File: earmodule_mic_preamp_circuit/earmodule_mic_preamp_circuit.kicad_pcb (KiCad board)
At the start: 2 copper layers, 43.8 x 25.4 mm, 53 parts, among them CN1 22uF, U100 AD8476ARMZ, U200 AD8476ARMZ, U300 ADA4661-2ARMZ, U400 TITLV71210

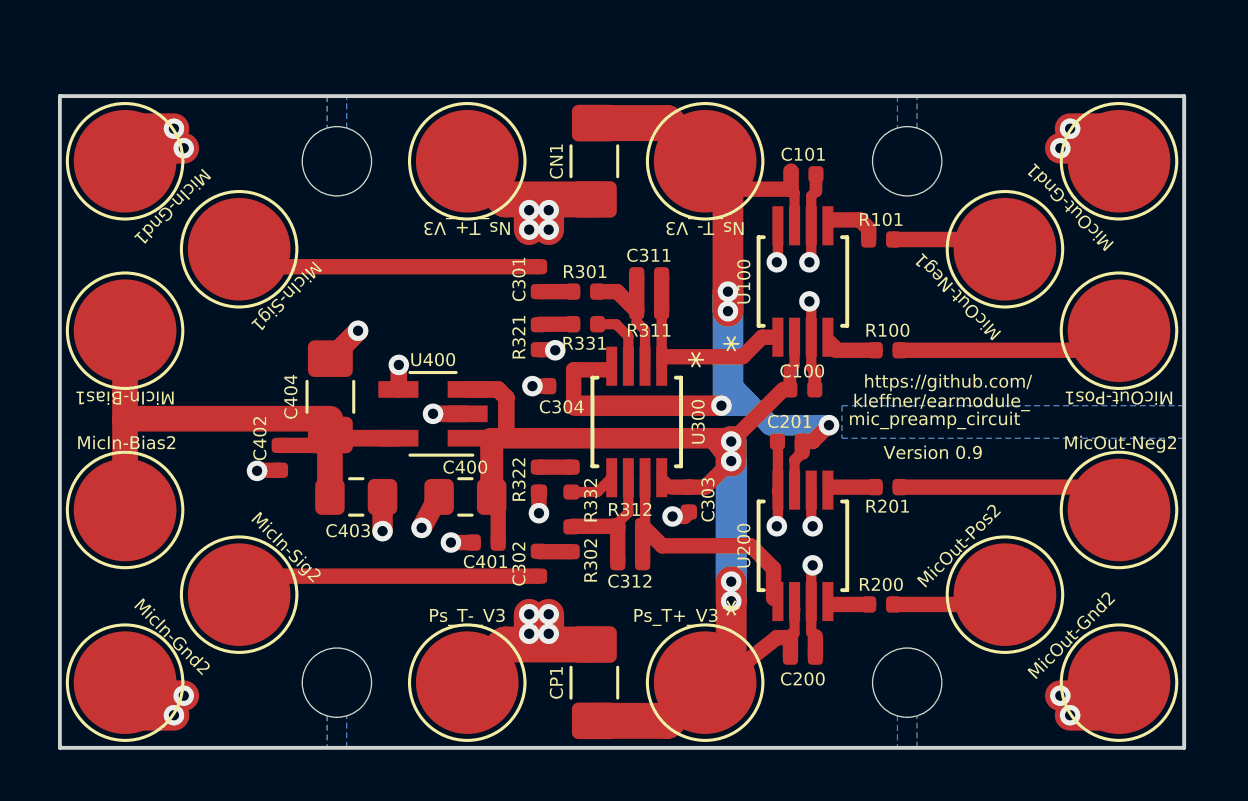
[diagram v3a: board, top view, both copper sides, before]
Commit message: Corrected miminum solder mask width. Aligned traces and copper fill along board edge to statisfy minimums. Removed backup file from repo.
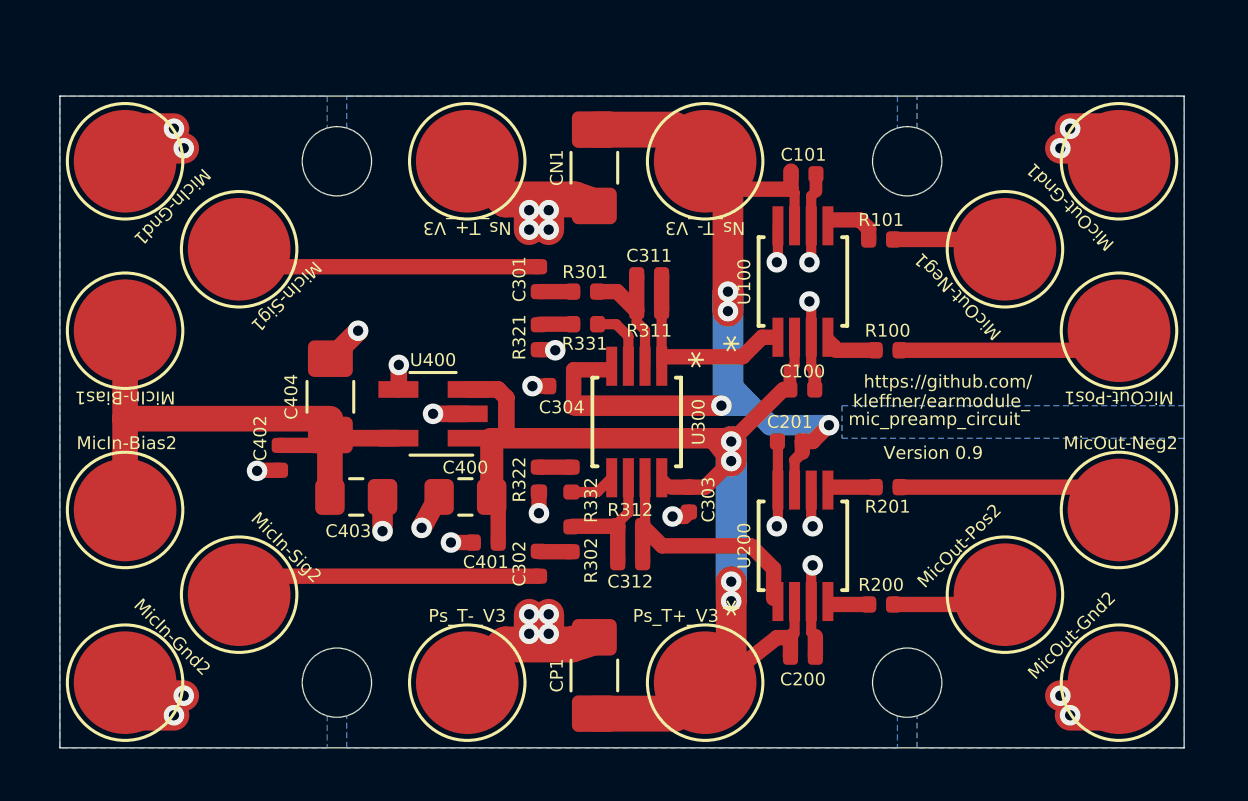
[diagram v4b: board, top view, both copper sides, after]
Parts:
- moved CP1 0.28 mm to (126.5, 94.5)
- moved CN1 0.25 mm to (126.5, 74.7)
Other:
- rule solder_mask_min_width: 0.25 -> 0.1016
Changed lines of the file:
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@@
     (thickness 1.6)
     (drawings 8)
-    (tracks 212)
+    (tracks 210)
     (zones 0)
     (modules 53)
@@
     (trace_min 0.2)
     (segment_width 0.2)
-    (edge_width 0.15)
+    (edge_width 0.05)
     (via_size 0.8)
     (via_drill 0.4)
@@
     (pad_drill 2.7)
     (pad_to_mask_clearance 0.051)
-    (solder_mask_min_width 0.25)
+    (solder_mask_min_width 0.1016)
     (aux_axis_origin 0 0)
     (visible_elements FFFDFF7F)
@@
   )
   (module Capacitor_SMD:C_1206_3216Metric_Pad1.42x1.75mm_HandSolder (layer F.Cu)
-    (at 126.492 74.422 90)
+    (at 126.492 74.676 90)
     (descr "Capacitor SMD 1206 (3216 Metric), square (rectangular) end terminal, IPC_7351 nominal with elongated pad for handsoldering. (Body size source: http://www.tortai-tech.com/upload/download/2011102023233369053.pdf), generated with kicad-footprint-generator")
     (tags "capacitor handsolder")
@@
   )
   (module Capacitor_SMD:C_1206_3216Metric_Pad1.42x1.75mm_HandSolder (layer F.Cu)
-    (at 126.492 94.742 90)
+    (at 126.492 94.461 90)
     (descr "Capacitor SMD 1206 (3216 Metric), square (rectangular) end terminal, IPC_7351 nominal with elongated pad for handsoldering. (Body size source: http://www.tortai-tech.com/upload/download/2011102023233369053.pdf), generated with kicad-footprint-generator")
     (tags "capacitor handsolder")
@@
     (effects (font (size 0.5 0.5) (thickness 0.0625)))
   )
-  (gr_line (start 149.479 71.882) (end 105.664 71.882) (layer Edge.Cuts) (width 0.15))
-  (gr_line (start 149.479 97.282) (end 149.479 71.882) (layer Edge.Cuts) (width 0.15))
-  (gr_line (start 105.664 97.282) (end 149.479 97.282) (layer Edge.Cuts) (width 0.15))
-  (gr_line (start 105.664 71.882) (end 105.664 97.282) (layer Edge.Cuts) (width 0.15))
+  (gr_line (start 149.479 71.882) (end 105.664 71.882) (layer Edge.Cuts) (width 0.05))
+  (gr_line (start 149.479 97.282) (end 149.479 71.882) (layer Edge.Cuts) (width 0.05))
+  (gr_line (start 105.664 97.282) (end 149.479 97.282) (layer Edge.Cuts) (width 0.05))
+  (gr_line (start 105.664 71.882) (end 105.664 97.282) (layer Edge.Cuts) (width 0.05))
   (segment (start 124.333 79.502) (end 125.649 79.502) (width 0.6) (layer F.Cu) (net 1))
   (segment (start 125.603 89.639) (end 124.333 89.639) (width 0.6) (layer F.Cu) (net 2))
@@
   (segment (start 137.183 77.05) (end 136.841 76.708) (width 0.6) (layer F.Cu) (net 8))
   (segment (start 137.183 77.47) (end 137.183 77.05) (width 0.6) (layer F.Cu) (net 8))
-  (segment (start 135.709299 91.694) (end 135.594999 91.5797) (width 0.4) (layer F.Cu) (net 9))
   (segment (start 137.183 91.694) (end 135.709299 91.694) (width 0.6) (layer F.Cu) (net 9))
-  (segment (start 135.709299 87.122) (end 135.594999 87.2363) (width 0.4) (layer F.Cu) (net 10))
   (segment (start 137.437 87.122) (end 135.709299 87.122) (width 0.6) (layer F.Cu) (net 10))
   (segment (start 124.356 80.772) (end 124.333 80.795) (width 0.4) (layer F.Cu) (net 11))
@@
   (segment (start 130.175 87.122) (end 130.81 87.122) (width 0.6) (layer F.Cu) (net 15))
   (segment (start 134.294999 92.827001) (end 134.294999 91.919665) (width 0.4) (layer F.Cu) (net 15))
-  (segment (start 134.294999 91.919665) (end 134.3291 91.885564) (width 0.4) (layer F.Cu) (net 15))
-  (segment (start 129.3225 96.2295) (end 130.81 94.742) (width 1.4) (layer F.Cu) (net 15))
-  (segment (start 126.492 96.2295) (end 129.3225 96.2295) (width 1.4) (layer F.Cu) (net 15))
   (segment (start 134.079001 92.964) (end 134.239 92.827001) (width 0.5) (layer F.Cu) (net 15))
   (segment (start 134.079001 92.987) (end 134.079001 92.964) (width 0.5) (layer F.Cu) (net 15))
@@
   (segment (start 133.604 92.987) (end 130.81 95.2) (width 0.6) (layer F.Cu) (net 15))
   (segment (start 122.7455 89.281) (end 122.7455 87.757) (width 0.6) (layer F.Cu) (net 15))
+  (segment (start 129.6035 95.9485) (end 130.81 94.742) (width 1.4) (layer F.Cu) (net 15))
+  (segment (start 126.492 95.9485) (end 129.6035 95.9485) (width 1.4) (layer F.Cu) (net 15))
   (segment (start 134.158 75.510601) (end 134.158 74.803) (width 0.6) (layer F.Cu) (net 16))
   (via (at 131.699 79.502) (size 0.8) (drill 0.4) (layers F.Cu B.Cu) (net 16))
@@
   (segment (start 134.294999 76.9366) (end 134.294999 75.6476) (width 0.4) (layer F.Cu) (net 16))
   (segment (start 131.699 79.502) (end 131.699 74.422) (width 1.2) (layer F.Cu) (net 16))
-  (segment (start 129.3225 72.9345) (end 130.81 74.422) (width 1.4) (layer F.Cu) (net 16))
-  (segment (start 126.492 72.9345) (end 129.3225 72.9345) (width 1.4) (layer F.Cu) (net 16))
+  (segment (start 129.5765 73.1885) (end 130.81 74.422) (width 1.4) (layer F.Cu) (net 16))
+  (segment (start 126.492 73.1885) (end 129.5765 73.1885) (width 1.4) (layer F.Cu) (net 16))
   (via (at 120.904 89.281) (size 0.8) (drill 0.4) (layers F.Cu B.Cu) (net 17))
   (via (at 113.3475 86.487) (size 0.8) (drill 0.4) (layers F.Cu B.Cu) (net 17))
@@
   (via (at 123.952 92.075) (size 0.8) (drill 0.4) (layers F.Cu B.Cu) (net 17))
   (via (at 124.714 76.327) (size 0.8) (drill 0.4) (layers F.Cu B.Cu) (net 17))
-  (segment (start 133.604 87.277301) (end 133.645001 87.2363) (width 0.4) (layer F.Cu) (net 17))
   (segment (start 133.645001 78.317999) (end 133.604 78.359) (width 0.4) (layer F.Cu) (net 17))
   (segment (start 133.645001 76.9366) (end 133.645001 78.317999) (width 0.4) (layer F.Cu) (net 17))
@@
   (segment (start 124.333 81.765) (end 124.945 81.765) (width 0.6) (layer F.Cu) (net 17))
   (segment (start 123.0265 93.2545) (end 121.539 94.742) (width 1.4) (layer F.Cu) (net 17))
-  (segment (start 126.492 93.2545) (end 123.0265 93.2545) (width 1.4) (layer F.Cu) (net 17))
+  (segment (start 125.603 93.2545) (end 123.0265 93.2545) (width 1.4) (layer F.Cu) (net 17))
   (segment (start 124.714 92.075) (end 124.714 92.837) (width 1.2) (layer F.Cu) (net 17))
   (segment (start 123.952 92.075) (end 123.952 92.837) (width 1.2) (layer F.Cu) (net 17))
   (segment (start 123.0265 75.9095) (end 121.539 74.422) (width 1.4) (layer F.Cu) (net 17))
-  (segment (start 126.492 75.9095) (end 123.0265 75.9095) (width 1.4) (layer F.Cu) (net 17))
+  (segment (start 125.703 75.9095) (end 123.0265 75.9095) (width 1.4) (layer F.Cu) (net 17))
   (segment (start 124.714 77.089) (end 124.714 76.327) (width 1.2) (layer F.Cu) (net 17))
   (segment (start 123.952 77.089) (end 123.952 76.327) (width 1.2) (layer F.Cu) (net 17))
@@
   (segment (start 119.761 88.7095) (end 120.4115 87.503) (width 0.8) (layer F.Cu) (net 17))
   (segment (start 121.7755 89.281) (end 120.904 89.281) (width 0.6) (layer F.Cu) (net 17))
+  (segment (start 126.4825 92.9735) (end 125.603 93.2545) (width 1.4) (layer F.Cu) (net 17))
+  (segment (start 126.4555 76.1635) (end 125.73 75.9095) (width 1.4) (layer F.Cu) (net 17))
   (segment (start 138.153 91.694) (end 142.494 91.694) (width 0.6) (layer F.Cu) (net 18))
   (segment (start 138.407 81.788) (end 146.939 81.788) (width 0.6) (layer F.Cu) (net 19))
